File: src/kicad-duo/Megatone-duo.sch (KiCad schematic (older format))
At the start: 22 parts, among them P1 Classic, P2 Boost, P3 Gnd, SW1 LORLIN_2X6

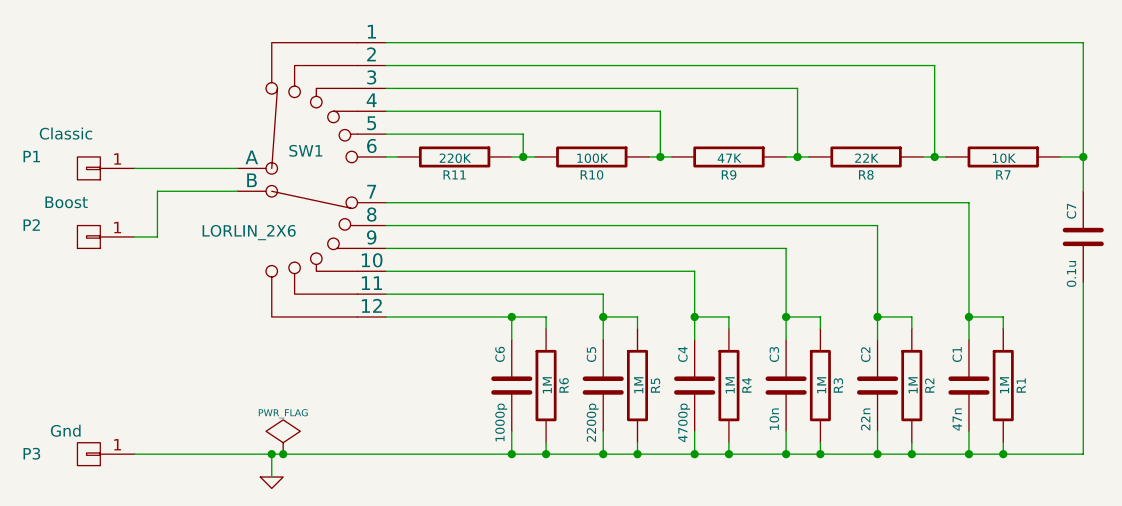
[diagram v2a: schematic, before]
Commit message: Turning output pins by 90°
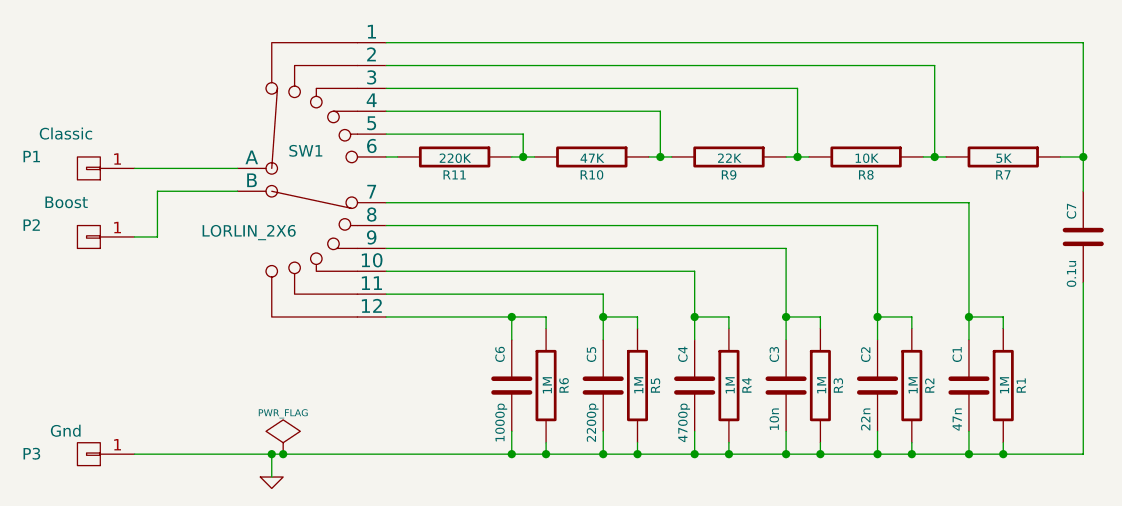
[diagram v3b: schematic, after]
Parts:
- R10: value 100K -> 47K
- R7: value 10K -> 5K
- R8: value 22K -> 10K
- R9: value 47K -> 22K
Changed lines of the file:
@@
 Sheet 1 1
 Title "Megatone Duo"
-Date "21 October 2014"
-Rev "v6"
+Date "04 April 2015"
+Rev "v6.2"
 Comp ""
 Comment1 "Open Hardware, Licensed under CERN OHL v1.2"
@@
 P 8700 4750
 F 0 "R10" V 8780 4750 40  0000 C CNN
-F 1 "100K" V 8707 4751 40  0000 C CNN
+F 1 "47K" V 8707 4751 40  0000 C CNN
 F 2 "libcms:SM0805" V 8630 4750 30  0001 C CNN
 F 3 "" H 8700 4750 30  0000 C CNN
@@
 P 9300 4750
 F 0 "R9" V 9380 4750 40  0000 C CNN
-F 1 "47K" V 9307 4751 40  0000 C CNN
+F 1 "22K" V 9307 4751 40  0000 C CNN
 F 2 "libcms:SM0805" V 9230 4750 30  0001 C CNN
 F 3 "" H 9300 4750 30  0000 C CNN
@@
 P 9900 4750
 F 0 "R8" V 9980 4750 40  0000 C CNN
-F 1 "22K" V 9907 4751 40  0000 C CNN
+F 1 "10K" V 9907 4751 40  0000 C CNN
 F 2 "libcms:SM0805" V 9830 4750 30  0001 C CNN
 F 3 "" H 9900 4750 30  0000 C CNN
@@
 P 10500 4750
 F 0 "R7" V 10580 4750 40  0000 C CNN
-F 1 "10K" V 10507 4751 40  0000 C CNN
+F 1 "5K" V 10507 4751 40  0000 C CNN
 F 2 "libcms:SM0805" V 10430 4750 30  0001 C CNN
 F 3 "" H 10500 4750 30  0000 C CNN
